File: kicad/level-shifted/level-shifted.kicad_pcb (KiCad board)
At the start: 4 copper layers, 54.6 x 59 mm, 27 parts, among them J101 Conn_01x09_Socket, J102 Conn_01x09_Socket, J103 Conn_01x09_Socket, J104 PAL-1 Expansion Connector, J105 Conn_01x09_Socket, J106 Conn_01x09_Socket, J107 Conn_01x09_Socket, J109 Conn_01x09_Socket, J110 Conn_01x09_Socket, SW101 PICO RESET, U101 TXS0108EPW, U102 TXS0108EPW, U103 TXS0108EPW, U104 Pico, U105 TXS0108EPW

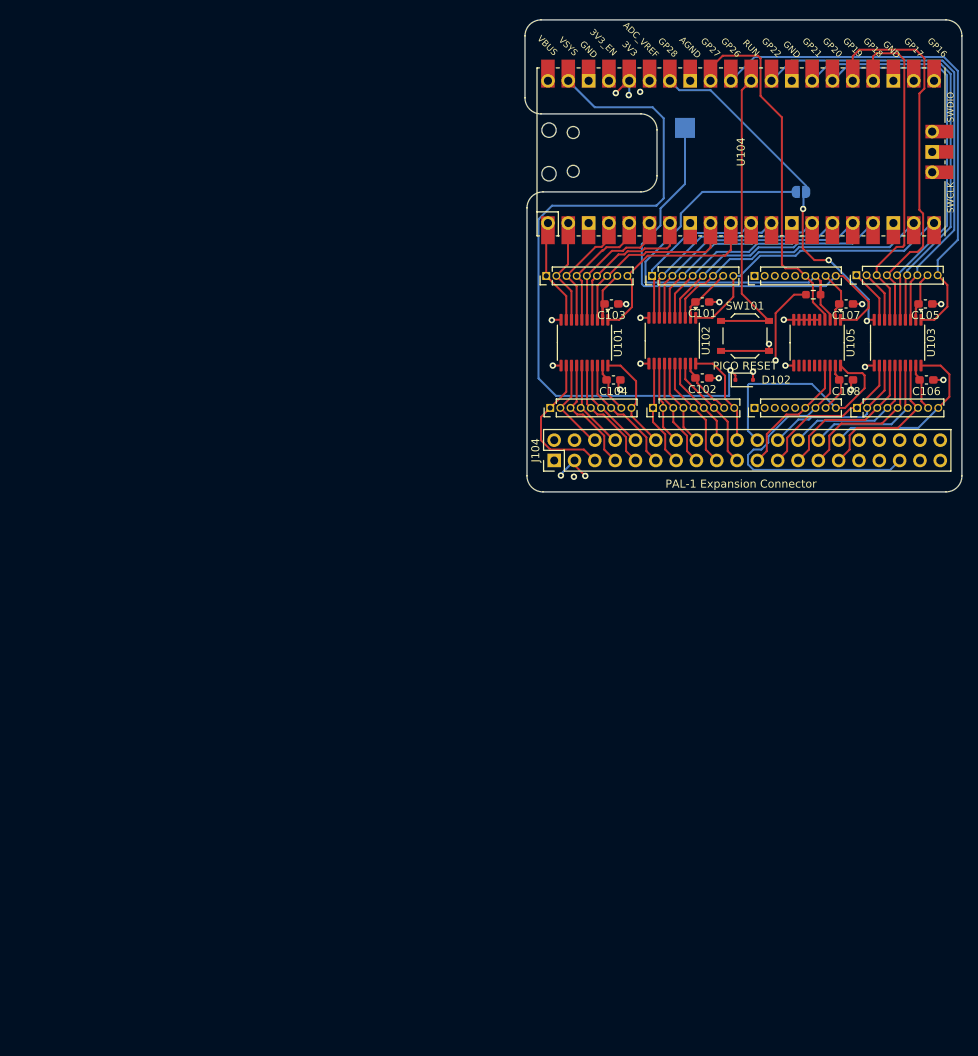
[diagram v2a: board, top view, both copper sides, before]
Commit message: PCB for the level shifted version
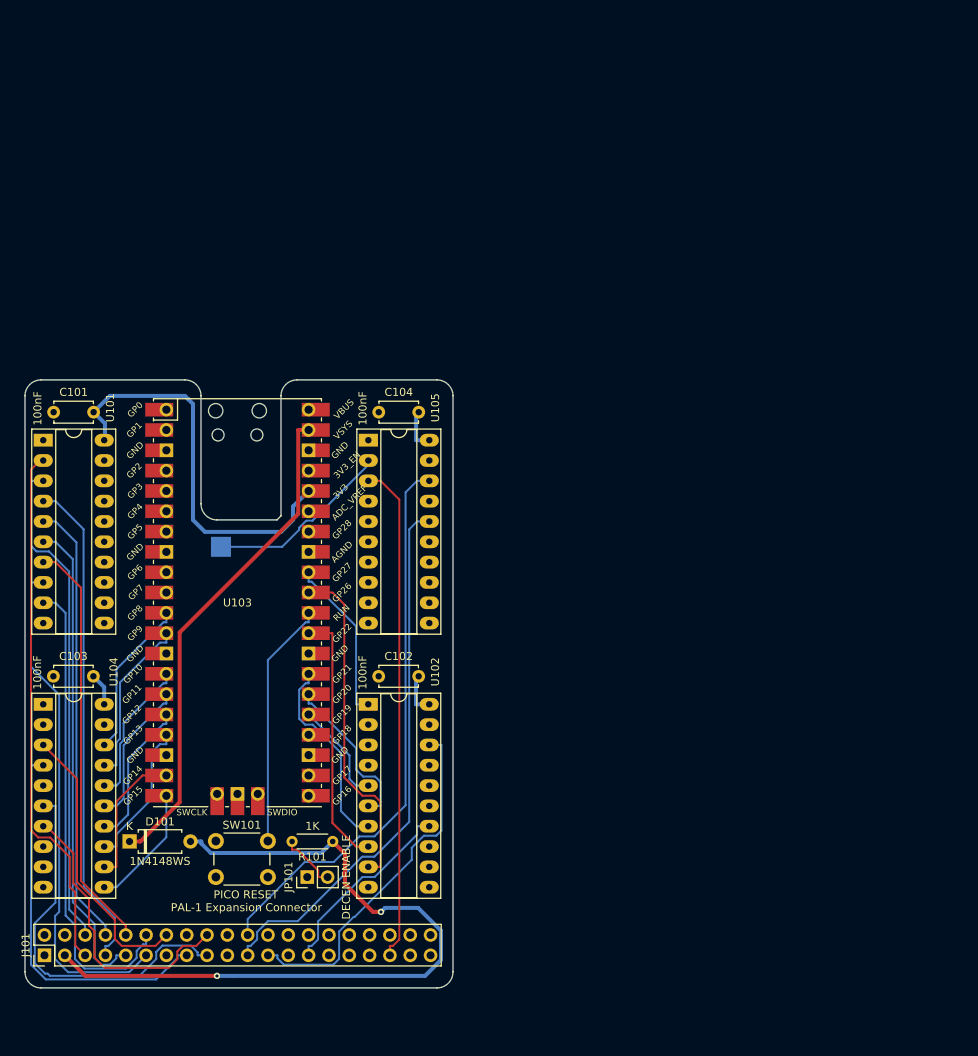
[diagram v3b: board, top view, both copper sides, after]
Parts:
- removed C105, C106, C107, C108: 0.1uf, Capacitor_SMD:C_0603_1608Metric_Pad1.08x0.95mm_HandSolder
- removed D102: 1N4148WS, Diode_SMD:D_SOD-323F
- removed J102, J103, J105, J106, J107, J109, J110: Conn_01x09_Socket, Connector_PinHeader_1.27mm:PinHeader_1x09_P1.27mm_Vertical
- removed J104: PAL-1 Expansion Connector, Connector_PinHeader_2.54mm:PinHeader_2x20_P2.54mm_Vertical
- added D101: 1N4148WS, Diode_THT:D_A-405_P7.62mm_Horizontal, F.Cu at (75.6, 163.2)
- C101, C102, C103, C104: value 0.1uf -> 100nF; footprint Capacitor_SMD:C_0603_1608Metric_Pad1.08x0.95mm_HandSolder -> Capacitor_THT:C_Disc_D4.7mm_W2.5mm_P5.00mm
- J101: value Conn_01x09_Socket -> PAL-1 Expansion Connector; footprint Connector_PinHeader_1.27mm:PinHeader_1x09_P1.27mm_Vertical -> Connector_PinHeader_2.54mm:PinHeader_2x20_P2.54mm_Vertical
- JP101: footprint Jumper:SolderJumper-2_P1.3mm_Open_RoundedPad1.0x1.5mm -> Connector_PinHeader_2.54mm:PinHeader_1x02_P2.54mm_Vertical; moved to F.Cu
- R101: footprint Resistor_SMD:R_0603_1608Metric_Pad0.98x0.95mm_HandSolder -> Resistor_THT:R_Axial_DIN0204_L3.6mm_D1.6mm_P5.08mm_Horizontal
- SW101: footprint Button_Switch_SMD:SW_Push_1P1T_XKB_TS-1187A -> Button_Switch_THT:SW_PUSH_6mm_H4.3mm
- U101, U102, U105: value TXS0108EPW -> 74LVC245; footprint Package_SO:TSSOP-20_4.4x6.5mm_P0.65mm -> Package_DIP:DIP-20_W7.62mm_Socket_LongPads
- U103: value TXS0108EPW -> Pico; footprint Package_SO:TSSOP-20_4.4x6.5mm_P0.65mm -> RPi_Pico:RPi_Pico_SMD_TH
- U104: value Pico -> 74LVC245; footprint RPi_Pico:RPi_Pico_SMD_TH -> Package_DIP:DIP-20_W7.62mm_Socket_LongPads
- moved J101 122.5 mm to (64.9, 177.4)
- moved U104 111.2 mm to (64.8, 146.1), turned to 0 degrees
- moved JP101 105.6 mm to (97.8, 167.6), turned to 90 degrees
- moved SW101 91.4 mm to (86.4, 163.1)
- moved R101 91.0 mm to (101.0, 163.2), turned to 180 degrees
- moved U103 88.7 mm to (89.1, 133.3), turned to 0 degrees
- moved C103 83.9 mm to (66.0, 142.5), turned to 0 degrees
- moved C101 82.2 mm to (66.1, 109.5), turned to 0 degrees
- moved TP101 78.1 mm to (87.0, 126.4)
- moved U101 68.7 mm to (64.8, 113.0), turned to 0 degrees
- moved U102 59.2 mm to (105.4, 146.1), turned to 0 degrees
- moved U105 57.4 mm to (105.4, 113.0), turned to 0 degrees
- moved C102 55.0 mm to (106.7, 142.5), turned to 0 degrees
- moved C104 29.6 mm to (106.7, 109.5), turned to 0 degrees
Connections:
- C101 pad 2: 3V3 -> +3.3V
- C102 pad 2: 5V -> +3.3V
- C103 pad 2: 3V3 -> +3.3V
- C104 pad 2: 5V -> +3.3V
- J101 pad 1: HVD0 -> GND
- J101 pad 2: HVD1 -> GND
- J101 pad 3: HVD2 -> V5
- J101 pad 4: HVD3 -> unconnected-(J101-~{RESET}-Pad4)
- J101 pad 5: HVD4 -> /HVA0
- J101 pad 6: HVD5 -> /HVA1
- J101 pad 7: HVD6 -> /HVA2
- J101 pad 8: 5V -> /HVA3
- J101 pad 9: HVD7 -> /HVA4
- JP101 pad 2: LVDEN -> /~{LVDEN}
- R101 pad 1: 5V -> V5
- R101 pad 2: LVDEN -> /~{LVDEN}
- U101 pad 1: /LVA7 -> +3.3V
- U101 pad 10: 3V3 -> GND
- U101 pad 11: GND -> /LVA7
- U101 pad 12: /HVA0 -> /LVA6
- U101 pad 13: /HVA1 -> /LVA5
- U101 pad 14: /HVA2 -> /LVA4
- U101 pad 15: /HVA3 -> /LVA3
- U101 pad 16: /HVA4 -> /LVA2
- U101 pad 17: /HVA5 -> /LVA1
- U101 pad 18: /HVA6 -> /LVA0
- U101 pad 19: 5V -> GND
- U101 pad 2: 3V3 -> /HVA0
- U101 pad 20: /HVA7 -> +3.3V
- U101 pad 3: /LVA6 -> /HVA1
- U101 pad 4: /LVA5 -> /HVA2
- U101 pad 5: /LVA4 -> /HVA3
- U101 pad 6: /LVA3 -> /HVA4
- U101 pad 7: /LVA2 -> /HVA5
- U101 pad 8: /LVA1 -> /HVA6
- U101 pad 9: /LVA0 -> /HVA7
- U102 pad 1: /LVA15 -> /LVR~{W}
- U102 pad 10: 3V3 -> GND
- U102 pad 11: GND -> /HVD7
- U102 pad 12: /HVA8 -> /HVD6
- U102 pad 13: /HVA9 -> /HVD5
- U102 pad 14: /HVA10 -> /HVD4
- U102 pad 15: /HVA11 -> /HVD3
- U102 pad 16: /HVA12 -> /HVD2
- U102 pad 17: /HVA13 -> /HVD1
- U102 pad 18: /HVA14 -> /HVD0
- U102 pad 19: 5V -> GND
- U102 pad 2: 3V3 -> /LVD0
- U102 pad 20: /HVA15 -> +3.3V
- U102 pad 3: /LVA14 -> /LVD1
- U102 pad 4: /LVA13 -> /LVD2
- U102 pad 5: /LVA12 -> /LVD3
- U102 pad 6: /LVA11 -> /LVD4
- U102 pad 7: /LVA10 -> /LVD5
- U102 pad 8: /LVA9 -> /LVD6
- U102 pad 9: /LVA8 -> /LVD7
- U103 pad 1: LVD7 -> /LVA0
- U103 pad 10: /DEN -> /LVA7
- U103 pad 11: GND -> /LVA8
- U103 pad 12: HVD0 -> /LVA9
- U103 pad 13: HVD1 -> GND
- U103 pad 14: HVD2 -> /LVA10
- U103 pad 15: HVD3 -> /LVA11
- U103 pad 16: HVD4 -> /LVA12
- U103 pad 17: HVD5 -> /LVA13
- U103 pad 18: HVD6 -> GND
- U103 pad 19: 5V -> /LVA14
- U103 pad 2: 3V3 -> /LVA1
- U103 pad 20: HVD7 -> /LVA15
- U103 pad 3: LVD6 -> GND
- U103 pad 4: LVD5 -> /LVA2
- U103 pad 5: LVD4 -> /LVA3
- U103 pad 6: LVD3 -> /LVA4
- U103 pad 7: LVD2 -> /LVA5
- U103 pad 8: LVD1 -> GND
- U103 pad 9: LVD0 -> /LVA6
- U104 pad 1: /LVA0 -> +3.3V
- U104 pad 10: /LVA7 -> GND
- U104 pad 11: /LVA8 -> /LVA15
- U104 pad 12: /LVA9 -> /LVA14
- U104 pad 13: GND -> /LVA13
- U104 pad 14: /LVA10 -> /LVA12
- U104 pad 16: /LVA12 -> /LVA10
- U104 pad 17: /LVA13 -> /LVA9
- U104 pad 18: GND -> /LVA8
- U104 pad 19: /LVA14 -> GND
- U104 pad 2: /LVA1 -> /HVA8
- U104 pad 20: /LVA15 -> +3.3V
- U104 pad 3: GND -> /HVA9
- U104 pad 4: /LVA2 -> /HVA10
- U104 pad 5: /LVA3 -> /HVA11
- U104 pad 6: /LVA4 -> /HVA12
- U104 pad 7: /LVA5 -> /HVA13
- U104 pad 8: GND -> /HVA14
- U104 pad 9: /LVA6 -> /HVA15
- U105 pad 1: LVPHI2 -> +3.3V
- U105 pad 10: 3V3 -> GND
- U105 pad 11: GND -> unconnected-(U105-B7-Pad11)
- U105 pad 16: unconnected-(U105-B4-Pad16) -> /HVR~{W}
- U105 pad 17: HVRW -> /~{LVDEN}
- U105 pad 18: HVDEN -> /HVPHI2
- U105 pad 19: 5V -> GND
- U105 pad 2: 3V3 -> LVPHI2
- U105 pad 20: HVPHI2 -> +3.3V
- U105 pad 3: LVDEN -> /~{HVDEN}
- U105 pad 4: LVRW -> /LVR~{W}
- U105 pad 5: 3V3 -> unconnected-(U105-A3-Pad5)
- U105 pad 6: 3V3 -> unconnected-(U105-A4-Pad6)
- U105 pad 7: 3V3 -> unconnected-(U105-A5-Pad7)
- U105 pad 8: 3V3 -> unconnected-(U105-A6-Pad8)
- U105 pad 9: 3V3 -> unconnected-(U105-A7-Pad9)
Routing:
- net +3.3V: track 0.00 -> 159.7 mm
- net V5: track 0.00 -> 92.5 mm, vias 0 -> 2
- net Net-(D102-K): track 90.0 -> 0.00 mm, vias 1 -> 0
- net /HVPHI2: track 0.00 -> 70.3 mm
- net /HVR~{W}: track 0.00 -> 67.8 mm
- net LVD7: track 65.3 -> 0.00 mm
- net /~{HVDEN}: track 0.00 -> 62.5 mm
- net /VSYS: track 0.00 -> 62.3 mm
- net /~{LVDEN}: track 0.00 -> 61.8 mm
- net LVD6: track 57.7 -> 0.00 mm
- net LVDEN: track 55.8 -> 0.00 mm
- net LVD5: track 51.8 -> 0.00 mm
- net /HVA1: track 11.8 -> 62.0 mm
- net LVD3: track 48.8 -> 0.00 mm
- net LVD4: track 48.7 -> 0.00 mm
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- removed copper zone on In2.Cu, net 3V3
- removed copper zone on In2.Cu, net 5V
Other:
- board size 54.6 x 59 mm -> 53.5 x 76 mm
- board text added: "WIDE BUS (VERSION 2.0)"
- board text added: "https://github.com/ JeremyJStarcher/ pal1-ram-rom"
- board text removed: "CONNECT TP101 TO TP5 ON PICO."
- board text removed: "PAL-1 RAM / ROM / TIMER BOARD SOFTWARE DEFINED https://github.com/JeremyJStarcher/pal1-ram-rom"

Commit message: Trial of multiplexed code
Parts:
- removed R101: 1K, Resistor_THT:R_Axial_DIN0204_L3.6mm_D1.6mm_P5.08mm_Horizontal
- added C105: 100nF, Capacitor_SMD:C_1812_4532Metric_Pad1.57x3.40mm_HandSolder, B.Cu at (91.0, 132.5)
- added J102: PAL-1 Expansion Connector, Connector_PinHeader_2.54mm:PinHeader_2x20_P2.54mm_Vertical, F.Cu at (64.7, 185.0)
- added U106: 74LS00, Package_DIP:DIP-14_W8.89mm_SMDSocket_LongPads, B.Cu at (89.9, 145.4)
- moved D101 10.9 mm to (86.5, 163.5)
- moved SW101 10.1 mm to (76.2, 163.2)
- moved JP101 3.28 mm to (98.7, 164.5)
- moved TP101 3.24 mm to (83.8, 127.0), turned to 90 degrees
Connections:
- JP101 pad 1: /DEN -> /~{DEN_S}
- JP101 pad 2: /~{LVDEN} -> /~{HVDEN}
- TP101 pad 1: LVPHI2 -> /HVPHI2
- U102 pad 1: /LVR~{W} -> /~{HV_W}
- U102 pad 19: GND -> /DATA_EN
- U103 pad 32: /LVR~{W} -> /~{LV_W}
- U103 pad 34: /DEN -> /~{LVDEN}
- U105 pad 1: +3.3V -> GND
- U105 pad 15: unconnected-(U105-B3-Pad15) -> /~{HV_W}
- U105 pad 2: LVPHI2 -> unconnected-(U105-A0-Pad2)
- U105 pad 3: /~{HVDEN} -> /~{DEN_S}
- U105 pad 4: /LVR~{W} -> unconnected-(U105-A2-Pad4)
- U105 pad 5: unconnected-(U105-A3-Pad5) -> /~{LV_W}
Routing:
- net /~{DEN_S}: track 0.00 -> 72.6 mm
- net /DATA_EN: track 0.00 -> 59.5 mm
- net V5: track 92.5 -> 142.0 mm, vias 2 -> 0
- net /HVPHI2: track 70.3 -> 118.9 mm
- net /DEN: track 46.3 -> 0.00 mm
- net +3.3V: track 159.7 -> 201.2 mm
- net /~{HV_W}: track 0.00 -> 38.5 mm
- net /~{HVDEN}: track 62.5 -> 24.7 mm
- net /HVR~{W}: track 67.8 -> 103.1 mm
- net /LVR~{W}: track 34.1 -> 0.00 mm
- net LVPHI2: track 23.4 -> 0.00 mm
- net GND: track 0.00 -> 22.8 mm
- net /HVA0: track 66.4 -> 86.7 mm
- net /HVA14: track 32.9 -> 50.4 mm
- net /~{LVDEN}: track 61.8 -> 44.3 mm
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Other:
- board size 53.5 x 76 mm -> 54 x 83 mm
- board text added: "WIDE BUS (VERSION 3.0)"
- board text added: "https://github.com/JeremyJStarcher/pal1-ram-rom"
- board text removed: "WIDE BUS (VERSION 2.0)"
- board text removed: "https://github.com/ JeremyJStarcher/ pal1-ram-rom"
